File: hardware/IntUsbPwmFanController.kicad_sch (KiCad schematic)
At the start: 40 parts, among them J1 UsbPortA, J2 UsbPortB, J3 MOLEX, J4 VselA, J5 VselB, J6 FAN, J7 USB_Out, J8 UDPI UART, Q1 IRLML6402, U2 FT201XS, U3 ATtiny202-SS

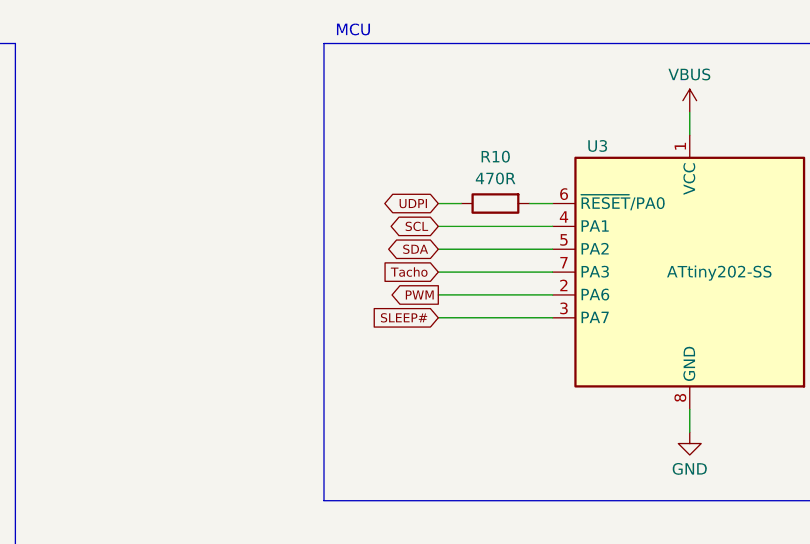
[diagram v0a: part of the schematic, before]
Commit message: Re-assign MCU pins after firmware considerations
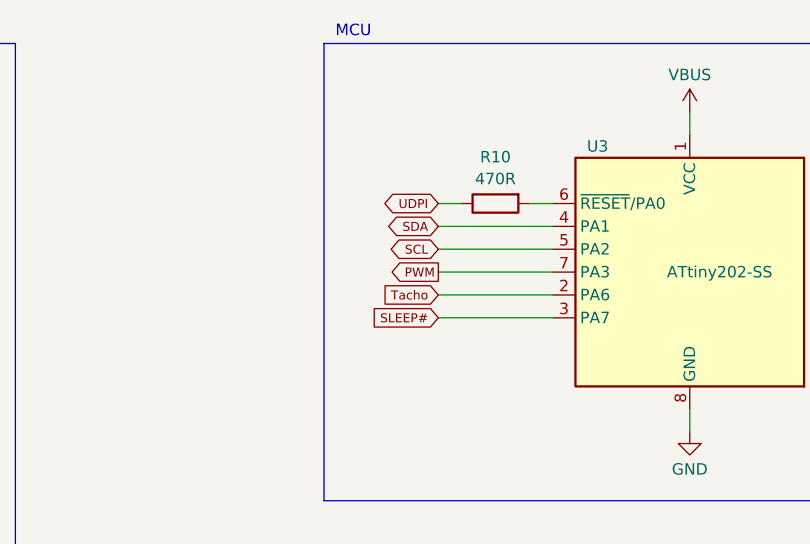
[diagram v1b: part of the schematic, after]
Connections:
- net PWM: now also U3.7 (PA3); no longer U3.2 (PA6)
- net SCL: now also U3.5 (PA2); no longer U3.4 (PA1)
- net SDA: now also U3.4 (PA1); no longer U3.5 (PA2)
- net Tacho: now also U3.2 (PA6); no longer U3.7 (PA3)
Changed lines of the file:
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@@
 	(global_label "SDA"
 		(shape bidirectional)
-		(at 186.69 40.64 180)
-		(fields_autoplaced yes)
-		(effects
-			(font
-				(size 1 1)
-			)
-			(justify right)
-		)
-		(property "Intersheetrefs" "${INTERSHEET_REFS}"
-			(at 180.6552 40.64 0)
+		(at 186.69 38.1 180)
+		(fields_autoplaced yes)
+		(effects
+			(font
+				(size 1 1)
+			)
+			(justify right)
+		)
+		(property "Intersheetrefs" "${INTERSHEET_REFS}"
+			(at 180.6552 38.1 0)
 			(effects
 				(font
@@
 	(global_label "PWM"
 		(shape output)
-		(at 186.69 45.72 180)
-		(fields_autoplaced yes)
-		(effects
-			(font
-				(size 1 1)
-			)
-			(justify right)
-		)
-		(property "Intersheetrefs" "${INTERSHEET_REFS}"
-			(at 181.0539 45.72 0)
+		(at 186.69 43.18 180)
+		(fields_autoplaced yes)
+		(effects
+			(font
+				(size 1 1)
+			)
+			(justify right)
+		)
+		(property "Intersheetrefs" "${INTERSHEET_REFS}"
+			(at 181.0539 43.18 0)
 			(effects
 				(font
@@
 	(global_label "SCL"
 		(shape bidirectional)
-		(at 186.69 38.1 180)
-		(fields_autoplaced yes)
-		(effects
-			(font
-				(size 1 1)
-			)
-			(justify right)
-		)
-		(property "Intersheetrefs" "${INTERSHEET_REFS}"
-			(at 180.7028 38.1 0)
+		(at 186.69 40.64 180)
+		(fields_autoplaced yes)
+		(effects
+			(font
+				(size 1 1)
+			)
+			(justify right)
+		)
+		(property "Intersheetrefs" "${INTERSHEET_REFS}"
+			(at 180.7028 40.64 0)
 			(effects
 				(font
@@
 	(global_label "Tacho"
 		(shape input)
-		(at 186.69 43.18 180)
-		(fields_autoplaced yes)
-		(effects
-			(font
-				(size 1 1)
-			)
-			(justify right)
-		)
-		(property "Intersheetrefs" "${INTERSHEET_REFS}"
-			(at 180.0063 43.18 0)
-			(effects
-				(font
+		(at 186.69 45.72 180)
+		(fields_autoplaced yes)
+		(effects
+			(font
+				(size 1 1)
+			)
+			(justify right)
+		)
+		(property "Intersheetrefs" "${INTERSHEET_REFS}"
+			(at 180.0063 45.72 0)
+			(effects
+				(font

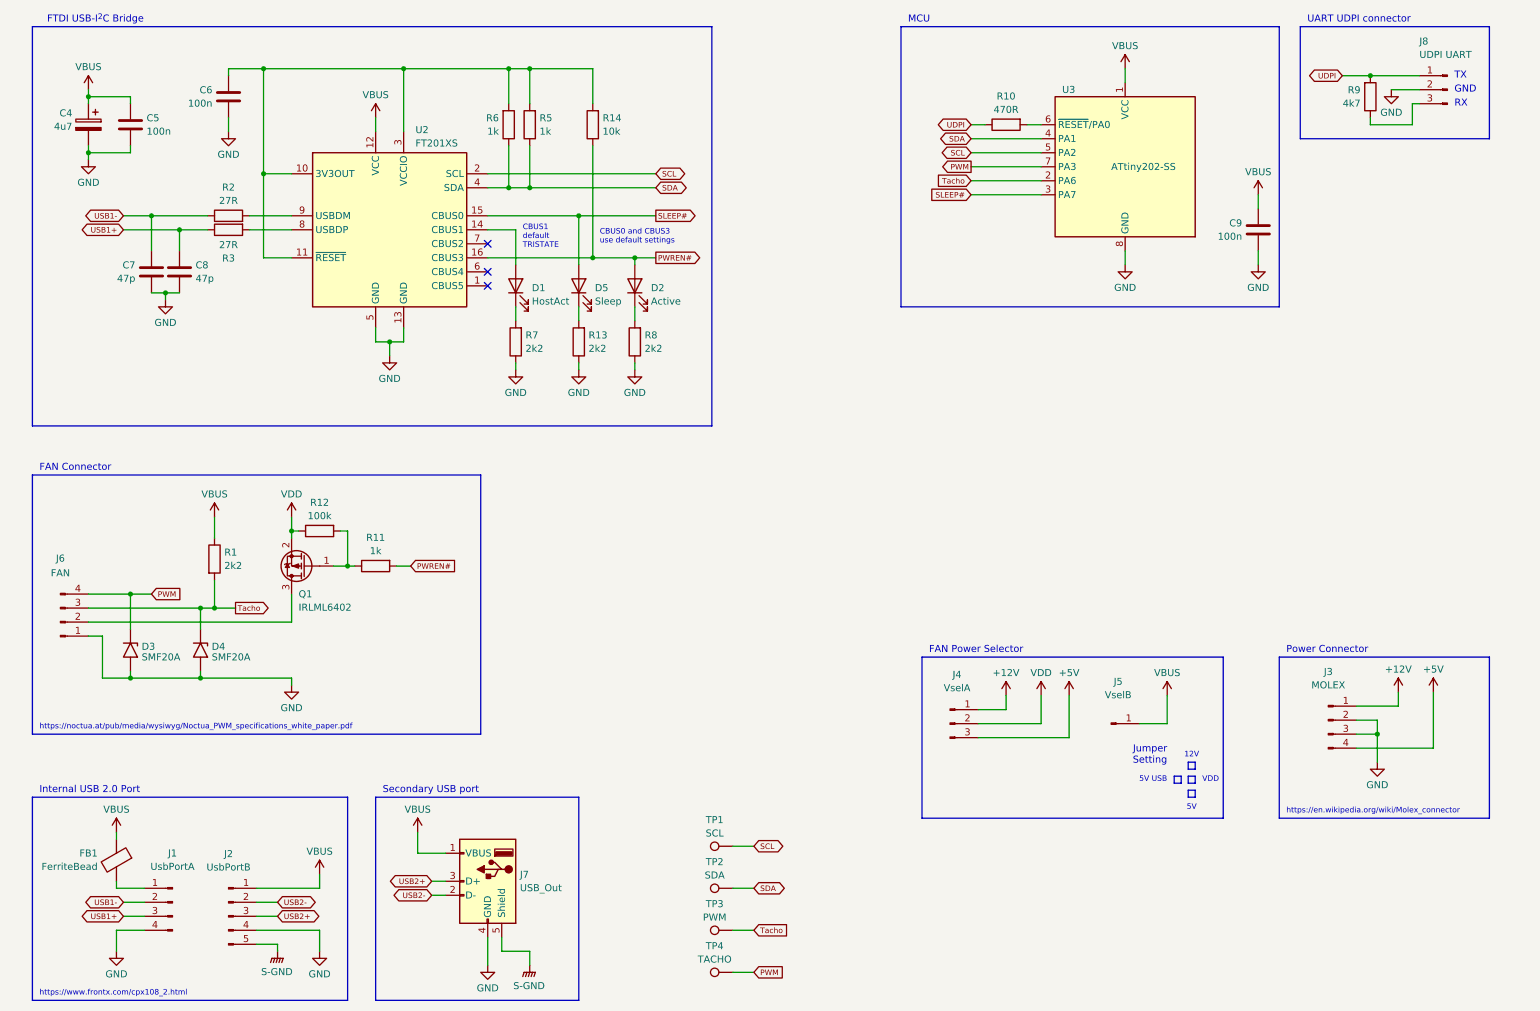
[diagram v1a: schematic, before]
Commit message: Replace FT201XS (I2C slave) with FT260S (I2C master)
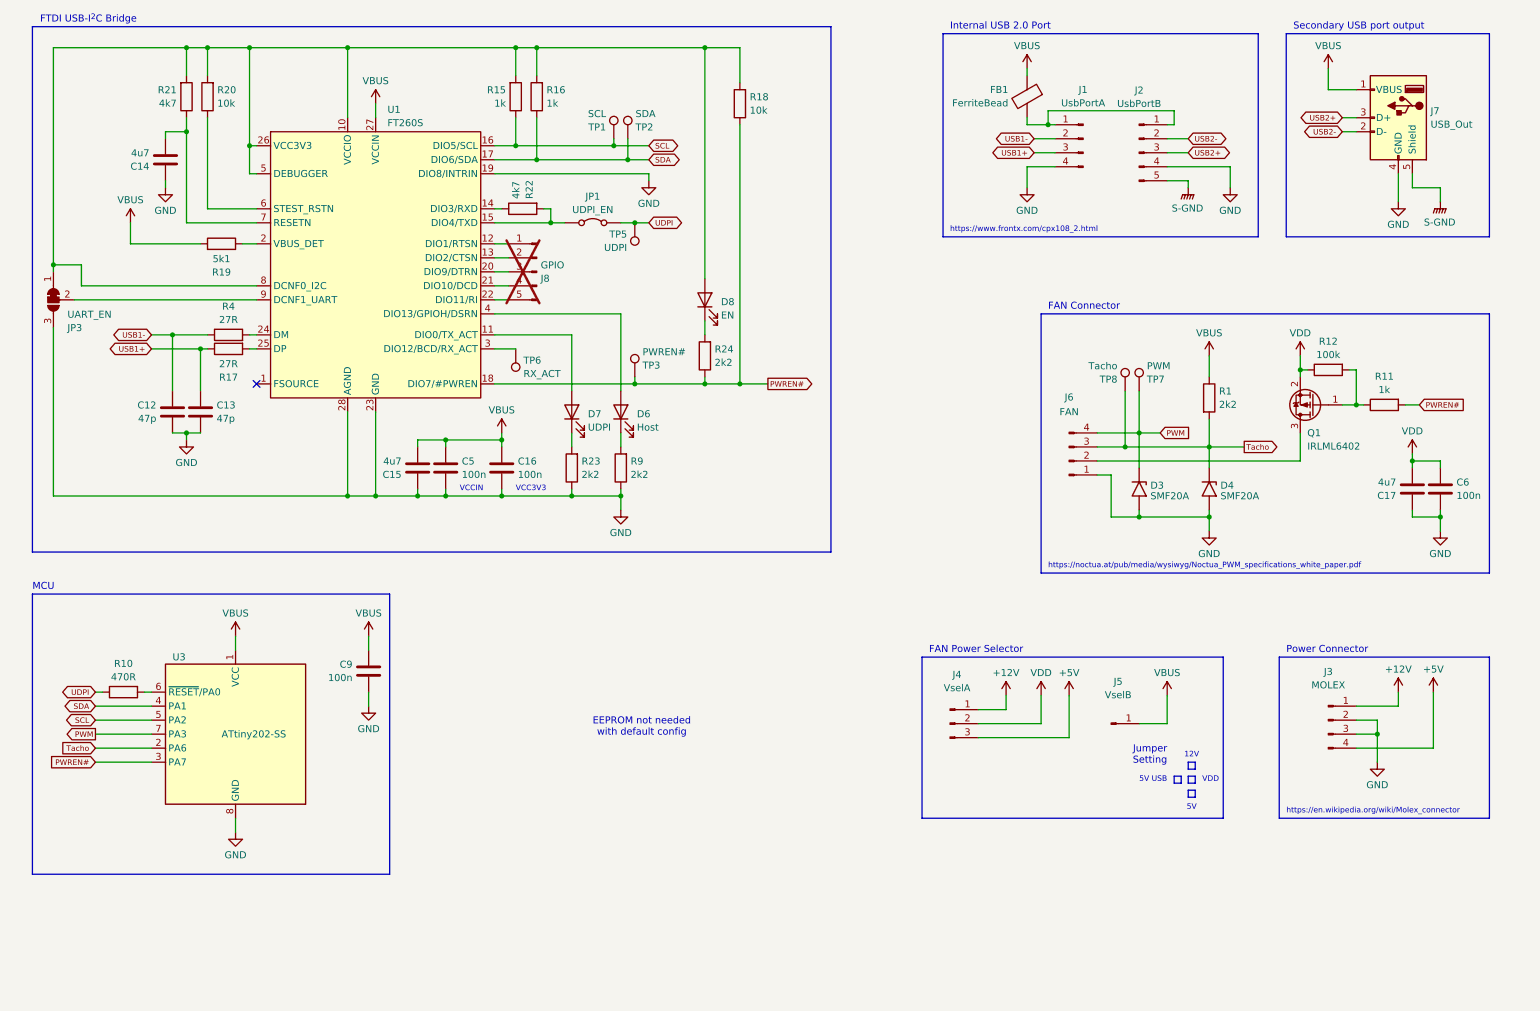
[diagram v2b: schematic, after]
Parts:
- removed C4: 4u7, Capacitor_SMD:C_0603_1608Metric_Pad1.08x0.95mm_HandSolder, symbol Device:C_Polarized
- removed C7, C8: 47p, Capacitor_SMD:C_0603_1608Metric_Pad1.08x0.95mm_HandSolder, symbol Device:C
- removed D1: HostAct, LED_SMD:LED_0603_1608Metric_Pad1.05x0.95mm_HandSolder, symbol Device:LED
- removed D2: Active, LED_SMD:LED_0603_1608Metric_Pad1.05x0.95mm_HandSolder, symbol Device:LED
- removed D5: Sleep, LED_SMD:LED_0603_1608Metric_Pad1.05x0.95mm_HandSolder, symbol Device:LED
- removed J8: UDPI UART, Connector_PinHeader_2.54mm:PinHeader_1x03_P2.54mm_Vertical, symbol Connector:Conn_01x03_Pin
- removed R13, R7, R8: 2k2, Resistor_SMD:R_0603_1608Metric_Pad0.98x0.95mm_HandSolder, symbol Device:R
- removed R14: 10k, Resistor_SMD:R_0603_1608Metric_Pad0.98x0.95mm_HandSolder, symbol Device:R
- removed R2, R3: 27R, Resistor_SMD:R_0603_1608Metric_Pad0.98x0.95mm_HandSolder, symbol Device:R
- removed R5, R6: 1k, Resistor_SMD:R_0603_1608Metric_Pad0.98x0.95mm_HandSolder, symbol Device:R
- removed TP4: TACHO, TestPoint:TestPoint_Pad_D1.0mm, symbol Connector:TestPoint
- removed U2: FT201XS, Package_SO:SSOP-16_3.9x4.9mm_P0.635mm, symbol Interface_USB:FT201XS
- added C12, C13: 47p, Capacitor_SMD:C_0603_1608Metric_Pad1.08x0.95mm_HandSolder, symbol Device:C
- added C14, C15, C17: 4u7, Capacitor_SMD:C_0603_1608Metric_Pad1.08x0.95mm_HandSolder, symbol Device:C
- added C16: 100n, Capacitor_SMD:C_0603_1608Metric_Pad1.08x0.95mm_HandSolder, symbol Device:C
- added D6: Host, LED_SMD:LED_0603_1608Metric_Pad1.05x0.95mm_HandSolder, symbol Device:LED
- added D7: UDPI, LED_SMD:LED_0603_1608Metric_Pad1.05x0.95mm_HandSolder, symbol Device:LED
- added D8: EN, LED_SMD:LED_0603_1608Metric_Pad1.05x0.95mm_HandSolder, symbol Device:LED
- added J8: GPIO, Connector_PinHeader_2.54mm:PinHeader_1x05_P2.54mm_Vertical, symbol Connector:Conn_01x05_Pin
- added JP1: UDPI_EN, Jumper:SolderJumper-2_P1.3mm_Bridged_RoundedPad1.0x1.5mm, symbol Jumper:Jumper_2_Bridged
- added JP3: UART_EN, symbol Jumper:SolderJumper_3_Bridged12
- added R15, R16: 1k, Resistor_SMD:R_0603_1608Metric_Pad0.98x0.95mm_HandSolder, symbol Device:R
- added R17, R4: 27R, Resistor_SMD:R_0603_1608Metric_Pad0.98x0.95mm_HandSolder, symbol Device:R
- added R18, R20: 10k, Resistor_SMD:R_0603_1608Metric_Pad0.98x0.95mm_HandSolder, symbol Device:R
- added R19: 5k1, Resistor_SMD:R_0603_1608Metric_Pad0.98x0.95mm_HandSolder, symbol Device:R
- added R21, R22: 4k7, Resistor_SMD:R_0603_1608Metric_Pad0.98x0.95mm_HandSolder, symbol Device:R
- added R23, R24: 2k2, Resistor_SMD:R_0603_1608Metric_Pad0.98x0.95mm_HandSolder, symbol Device:R
- added TP5: UDPI, TestPoint:TestPoint_Pad_D1.0mm, symbol Connector:TestPoint
- added TP6: RX_ACT, TestPoint:TestPoint_Pad_D1.0mm, symbol Connector:TestPoint
- added TP7: PWM, TestPoint:TestPoint_Pad_D1.0mm, symbol Connector:TestPoint
- added TP8: Tacho, TestPoint:TestPoint_Pad_D1.0mm, symbol Connector:TestPoint
- added U1: FT260S, Package_SO:TSSOP-28_4.4x9.7mm_P0.65mm, symbol FTDI:FT260S
- R9: value 4k7 -> 2k2
- TP3: value PWM -> PWREN#
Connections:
- net SLEEP# is gone; now on net PWREN#: U3.3 (PA7)
- net GND: now also R9.1, C12.2, C13.2, C14.1, C15.1, C16.2, C17.1, JP3.3 (B), R23.1, U1.19 (DIO8/INTRIN), U1.23 (GND), U1.28 (AGND)
- net PWM: now also TP7.1
- net PWREN#: now also TP3.1, R18.1, R24.1, U1.18 (DIO7/#PWREN)
- net SCL: now also R15.1, U1.16 (DIO5/SCL)
- net SDA: now also R16.1, U1.17 (DIO6/SDA)
- net Tacho: now also TP8.1; no longer TP3.1
- net UDPI: now also JP1.2 (B), TP5.1; no longer R9.2
- net USB1+: now also C13.1, R17.1
- net USB1-: now also C12.1, R4.1
- net VBUS: now also C15.2, C16.1, R19.2, U1.27 (VCCIN); no longer J2.1 (Pin_1)
- net VDD: now also C6.1, C17.2
- net at FB1.2, J1.1 (Pin_1): now also J2.1 (Pin_1)
- new net: R22.1, U1.14 (DIO3/RXD)
- new net: JP1.1 (A), R22.2, U1.15 (DIO4/TXD)
- new net: D6.1 (K), R9.2
- new net: D7.1 (K), R23.2
- new net: D7.2 (A), U1.11 (DIO0/TX_ACT)
- new net: D8.2 (A), JP3.1 (A), R15.2, R16.2, R18.2, R20.2, R21.2, U1.10 (VCCIO), U1.26 (VCC3V3), U1.5 (DEBUGGER), U1.8 (DCNF0_I2C)
- new net: JP3.2 (C), U1.9 (DCNF1_UART)
- new net: R4.2, U1.24 (DM)
- new net: R19.1, U1.2 (VBUS_DET)
- new net: D6.2 (A), U1.4 (DIO13/GPIOH/DSRN)
- new net: D8.1 (K), R24.2
- new net: J8.1 (Pin_1), U1.12 (DIO1/RTSN)
- new net: J8.2 (Pin_2), U1.13 (DIO2/CTSN)
- new net: J8.3 (Pin_3), U1.20 (DIO9/DTRN)
- new net: J8.4 (Pin_4), U1.21 (DIO10/DCD)
- new net: J8.5 (Pin_5), U1.22 (DIO11/RI)
- new net: R17.2, U1.25 (DP)
- new net: TP6.1, U1.3 (DIO12/BCD/RX_ACT)
- new net: R20.1, U1.6 (STEST_RSTN)
- new net: C14.2, R21.1, U1.7 (RESETN)
- no-connect marks 3 -> 1
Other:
- note added: "EEPROM not needed with default config"
- note added: "Secondary USB port output"
- note added: "VCC3V3"
- note added: "VCCIN"
- note removed: "CBUS0 and CBUS3 use default settings"
- note removed: "CBUS1 default TRISTATE"
- note removed: "GND"
- note removed: "RX"
- note removed: "Secondary USB port"
- note removed: "TX"
- note removed: "UART UDPI connector"
- moved on the sheet: C5, C9, D3, D4, FB1, J1, J2, J6, J7, Q1, R1, R10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
